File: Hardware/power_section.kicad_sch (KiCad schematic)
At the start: 40 parts, among them U4 TLV743P, U5 LM62440-Q1, U6 TLV743P, U7 TLV743P

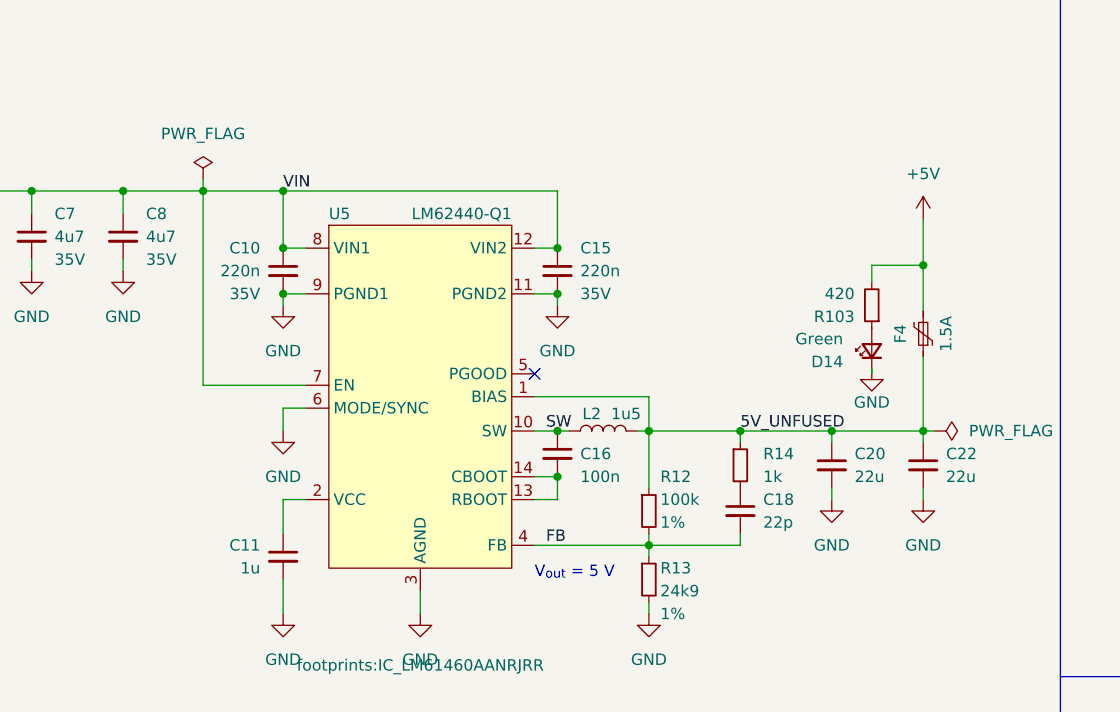
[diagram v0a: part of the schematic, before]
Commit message: Changes in current layout, added tensometers to layout
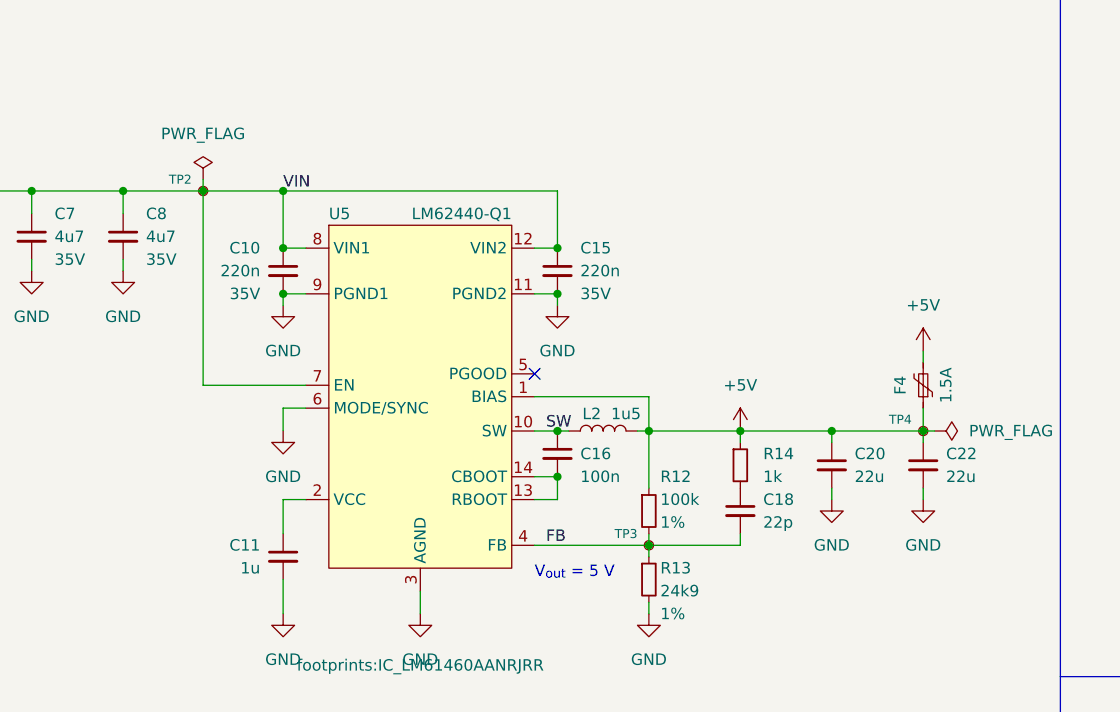
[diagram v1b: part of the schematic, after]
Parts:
- removed D14: Green, LED_SMD:LED_0603_1608Metric, symbol Device:LED_Small
- removed R103: 420, Resistor_SMD:R_0603_1608Metric, symbol Device:R_Small
- added TP2, TP3, TP4: TestPoint_Small, TestPoint:TestPoint_Pad_D1.0mm, symbol Connector:TestPoint_Small
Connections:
- net 5V_UNFUSED is gone; now on net +5V: C20.1, C22.1, F4.1, L2.2, R12.1, R14.1, U5.1 (BIAS)
- net +5V: now also TP4.1
- net FB: now also TP3.1
- net VIN: now also TP2.1
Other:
- moved on the sheet: F4

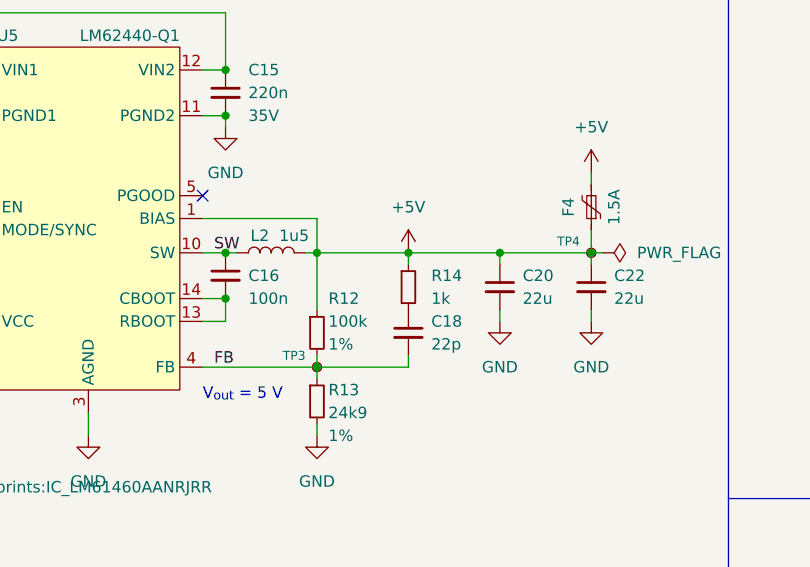
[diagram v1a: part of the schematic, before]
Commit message: Changes in power section
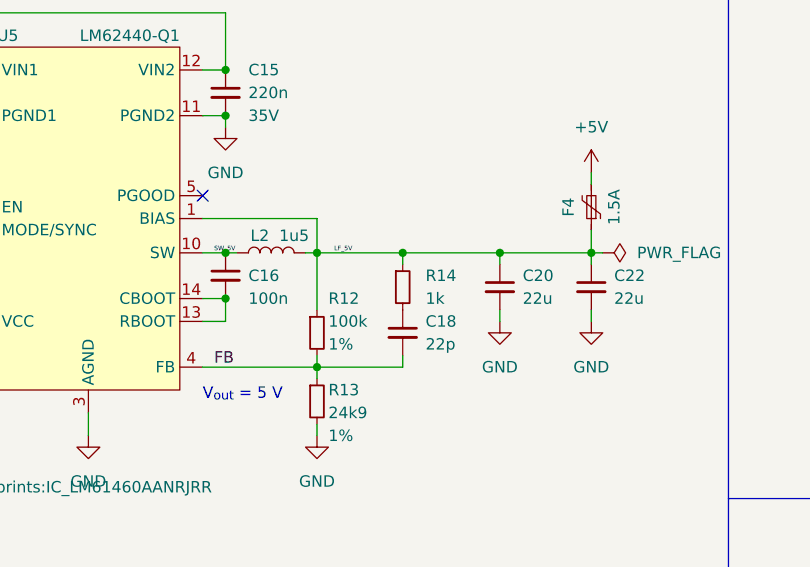
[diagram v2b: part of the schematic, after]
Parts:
- removed TP3, TP4: TestPoint_Small, TestPoint:TestPoint_Pad_D1.0mm, symbol Connector:TestPoint_Small
- TP2: footprint TestPoint:TestPoint_Pad_D1.0mm -> TestPoint:TestPoint_THTPad_D1.0mm_Drill0.5mm
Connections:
- net +5V: no longer C20.1, C22.1, F4.1, L2.2, R12.1, R14.1, U5.1 (BIAS)
- net SW renamed SW_5V
- new net LF_5V: C20.1, C22.1, F4.1, L2.2, R12.1, R14.1, U5.1 (BIAS)
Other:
- moved on the sheet: C18, R14
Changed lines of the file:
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@@
 	)
 	(junction
+		(at 140.97 64.77)
+		(diameter 0)
+		(color 0 0 0 0)
+	)
+	(junction
 		(at 58.42 158.75)
 		(diameter 0)
@@
 	)
 	(junction
-		(at 141.605 64.77)
-		(diameter 0)
-		(color 0 0 0 0)
-	)
-	(junction
 		(at 210.185 109.855)
 		(diameter 0)
@@
 	(wire
 		(pts
-			(xy 141.605 64.77) (xy 151.765 64.77)
-		)
-		(stroke
-			(width 0)
-			(type default)
-		)
-	)
-	(wire
-		(pts
 			(xy 195.58 116.205) (xy 195.58 116.84)
 		)
@@
 	(wire
 		(pts
-			(xy 141.605 64.77) (xy 141.605 66.04)
+			(xy 140.97 64.77) (xy 140.97 66.04)
 		)
 		(stroke
@@
 	(wire
 		(pts
+			(xy 140.97 64.77) (xy 151.765 64.77)
+		)
+		(stroke
+			(width 0)
+			(type default)
+		)
+	)
+	(wire
+		(pts
 			(xy 195.58 144.78) (xy 195.58 146.685)
 		)
@@
 	(wire
 		(pts
-			(xy 131.445 64.77) (xy 141.605 64.77)
+			(xy 131.445 64.77) (xy 140.97 64.77)
 		)
 		(stroke
@@
 	(wire
 		(pts
-			(xy 141.605 76.2) (xy 141.605 77.47)
+			(xy 140.97 76.2) (xy 140.97 77.47)
 		)
 		(stroke
@@
 	(wire
 		(pts
-			(xy 141.605 77.47) (xy 131.445 77.47)
+			(xy 140.97 77.47) (xy 131.445 77.47)
 		)
 		(stroke
@@
 		)
 	)
+	(label "LF_5V"
+		(at 133.35 64.77 0)
+		(fields_autoplaced yes)
+		(effects
+			(font
+				(size 0.5 0.5)
+			)
+			(justify left bottom)
+		)
+	)
 	(label "FB"
 		(at 120.015 77.47 0)
@@
 		)
 	)
-	(label "SW"
+	(label "SW_5V"
 		(at 120.015 64.77 0)
 		(fields_autoplaced yes)
 		(effects
 			(font
-				(size 1.27 1.27)
+				(size 0.5 0.5)
 			)
 			(justify left bottom)
@@
 	)
 	(symbol
-		(lib_id "power:+5V")
-		(at 141.605 64.77 0)
-		(unit 1)
-		(exclude_from_sim no)
-		(in_bom yes)
-		(on_board yes)
-		(dnp no)
-		(property "Reference" "#PWR0197"
-			(at 141.605 68.58 0)
-			(effects
-				(font
-					(size 1.27 1.27)
-				)
-				(hide yes)
-			)
-		)
-		(property "Value" "+5V"
-			(at 141.605 59.69 0)
-			(effects
-				(font
-					(size 1.27 1.27)
-				)
-			)
-		)
-		(property "Footprint" ""
-			(at 141.605 64.77 0)
-			(effects
-				(font
-					(size 1.27 1.27)
-				)
-				(hide yes)
-			)
-		)
-		(property "Datasheet" ""
-			(at 141.605 64.77 0)
-			(effects
-				(font
-					(size 1.27 1.27)
-				)
-				(hide yes)
-			)
-		)
-		(property "Description" ""
-			(at 141.605 64.77 0)
-			(effects
-				(font
-					(size 1.27 1.27)
-				)
-				(hide yes)
-			)
-		)
-		(pin "1"
-		)
-		(instances
-			(project "PUTM_EV_Frontbox_2023"
-				(path "/b652b05a-4e3d-4ad1-b032-18886abe7d45/fd3e8671-032e-4b6a-9a43-a9c36a92201e"
-					(reference "#PWR0197")
-					(unit 1)
-				)
-			)
-		)
-	)
-	(symbol
 		(lib_id "Regulator_Linear:TLV73330PDBV")
 		(at 220.345 147.32 0)
@@
 	)
 	(symbol
-		(lib_id "Connector:TestPoint_Small")
-		(at 161.925 64.77 0)
-		(unit 1)
-		(exclude_from_sim no)
-		(in_bom yes)
-		(on_board yes)
-		(dnp no)
-		(property "Reference" "TP4"
-			(at 160.655 63.5 0)
-			(effects
-				(font
-					(size 1 1)
-				)
-				(justify right)
-			)
-		)
-		(property "Value" "TestPoint_Small"
-			(at 163.195 66.675 0)
-			(effects
-				(font
-					(size 1.27 1.27)
-				)
-				(justify left)
-				(hide yes)
-			)
-		)
-		(property "Footprint" "TestPoint:TestPoint_Pad_D1.0mm"
-			(at 167.005 64.77 0)
-			(effects
-				(font
-					(size 1.27 1.27)
-				)
-				(hide yes)
-			)
-		)
-		(property "Datasheet" "~"
-			(at 167.005 64.77 0)
-			(effects
-				(font
-					(size 1.27 1.27)
-				)
-				(hide yes)
-			)
-		)
-		(property "Description" ""
-			(at 161.925 64.77 0)
-			(effects
-				(font
-					(size 1.27 1.27)
-				)
-				(hide yes)
-			)
-		)
-		(pin "1"
-		)
-		(instances
-			(project "PUTM_EV_Frontbox_2023"
-				(path "/b652b05a-4e3d-4ad1-b032-18886abe7d45/fd3e8671-032e-4b6a-9a43-a9c36a92201e"
-					(reference "TP4")
-					(unit 1)
-				)
-			)
-		)
-	)
-	(symbol
 		(lib_id "Regulator_Linear:TLV73330PDBV")
 		(at 47.625 161.29 0)
@@
 	(symbol
 		(lib_id "Device:R_Small")
-		(at 141.605 68.58 0)
+		(at 140.97 68.58 0)
 		(unit 1)
 		(exclude_from_sim no)
@@
 		(dnp no)
 		(property "Reference" "R14"
-			(at 144.145 67.31 0)
+			(at 143.51 67.31 0)
 			(effects
 				(font
@@
 		)
 		(property "Value" "1k"
-			(at 144.145 69.85 0)
+			(at 143.51 69.85 0)
 			(effects
 				(font
@@
 		)
 		(property "Footprint" "Resistor_SMD:R_0603_1608Metric"
-			(at 141.605 68.58 0)
+			(at 140.97 68.58 0)
 			(effects
 				(font
@@
 		)
 		(property "Datasheet" "~"
-			(at 141.605 68.58 0)
+			(at 140.97 68.58 0)
 			(effects
 				(font
@@
 		)
 		(property "Description" ""
-			(at 141.605 68.58 0)
+			(at 140.97 68.58 0)
 			(effects
 				(font
@@
 	)
 	(symbol
-		(lib_id "Connector:TestPoint_Small")
-		(at 131.445 77.47 0)
-		(unit 1)
-		(exclude_from_sim no)
-		(in_bom yes)
-		(on_board yes)
-		(dnp no)
-		(property "Reference" "TP3"
-			(at 130.175 76.2 0)
-			(effects
-				(font
-					(size 1 1)
-				)
-				(justify right)
-			)
-		)
-		(property "Value" "TestPoint_Small"
-			(at 132.715 79.375 0)
-			(effects
-				(font
-					(size 1.27 1.27)
-				)
-				(justify left)
-				(hide yes)
-			)
-		)
-		(property "Footprint" "TestPoint:TestPoint_Pad_D1.0mm"
-			(at 136.525 77.47 0)
-			(effects
-				(font
-					(size 1.27 1.27)
-				)
-				(hide yes)
-			)
-		)
-		(property "Datasheet" "~"
-			(at 136.525 77.47 0)
-			(effects
-				(font
-					(size 1.27 1.27)
-				)
-				(hide yes)
-			)
-		)
-		(property "Description" ""
-			(at 131.445 77.47 0)
-			(effects
-				(font
-					(size 1.27 1.27)
-				)
-				(hide yes)
-			)
-		)
-		(pin "1"
-		)
-		(instances
-			(project "PUTM_EV_Frontbox_2023"
-				(path "/b652b05a-4e3d-4ad1-b032-18886abe7d45/fd3e8671-032e-4b6a-9a43-a9c36a92201e"
-					(reference "TP3")
-					(unit 1)
-				)
-			)
-		)
-	)
-	(symbol
 		(lib_id "power:+5V")
 		(at 33.655 156.845 0)
@@
 			)
 		)
-		(property "Footprint" "TestPoint:TestPoint_Pad_D1.0mm"
+		(property "Footprint" "TestPoint:TestPoint_THTPad_D1.0mm_Drill0.5mm"
 			(at 86.995 38.1 0)
 			(effects
@@
 	(symbol
 		(lib_id "Device:C_Small")
-		(at 141.605 73.66 0)
+		(at 140.97 73.66 0)
 		(mirror y)
 		(unit 1)
@@
 		(dnp no)
 		(property "Reference" "C18"
-			(at 144.145 72.39 0)
+			(at 143.51 72.39 0)
 			(effects
 				(font
@@
 		)
 		(property "Value" "22p"
-			(at 144.145 74.93 0)
+			(at 143.51 74.93 0)
 			(effects
 				(font
@@
 		)
 		(property "Footprint" "Capacitor_SMD:C_0603_1608Metric"
-			(at 141.605 73.66 0)
+			(at 140.97 73.66 0)
 			(effects
 				(font
@@
 		)
 		(property "Datasheet" "~"
-			(at 141.605 73.66 0)
+			(at 140.97 73.66 0)
 			(effects
 				(font
@@
 		)
 		(property "Description" ""
-			(at 141.605 73.66 0)
+			(at 140.97 73.66 0)
 			(effects
 				(font

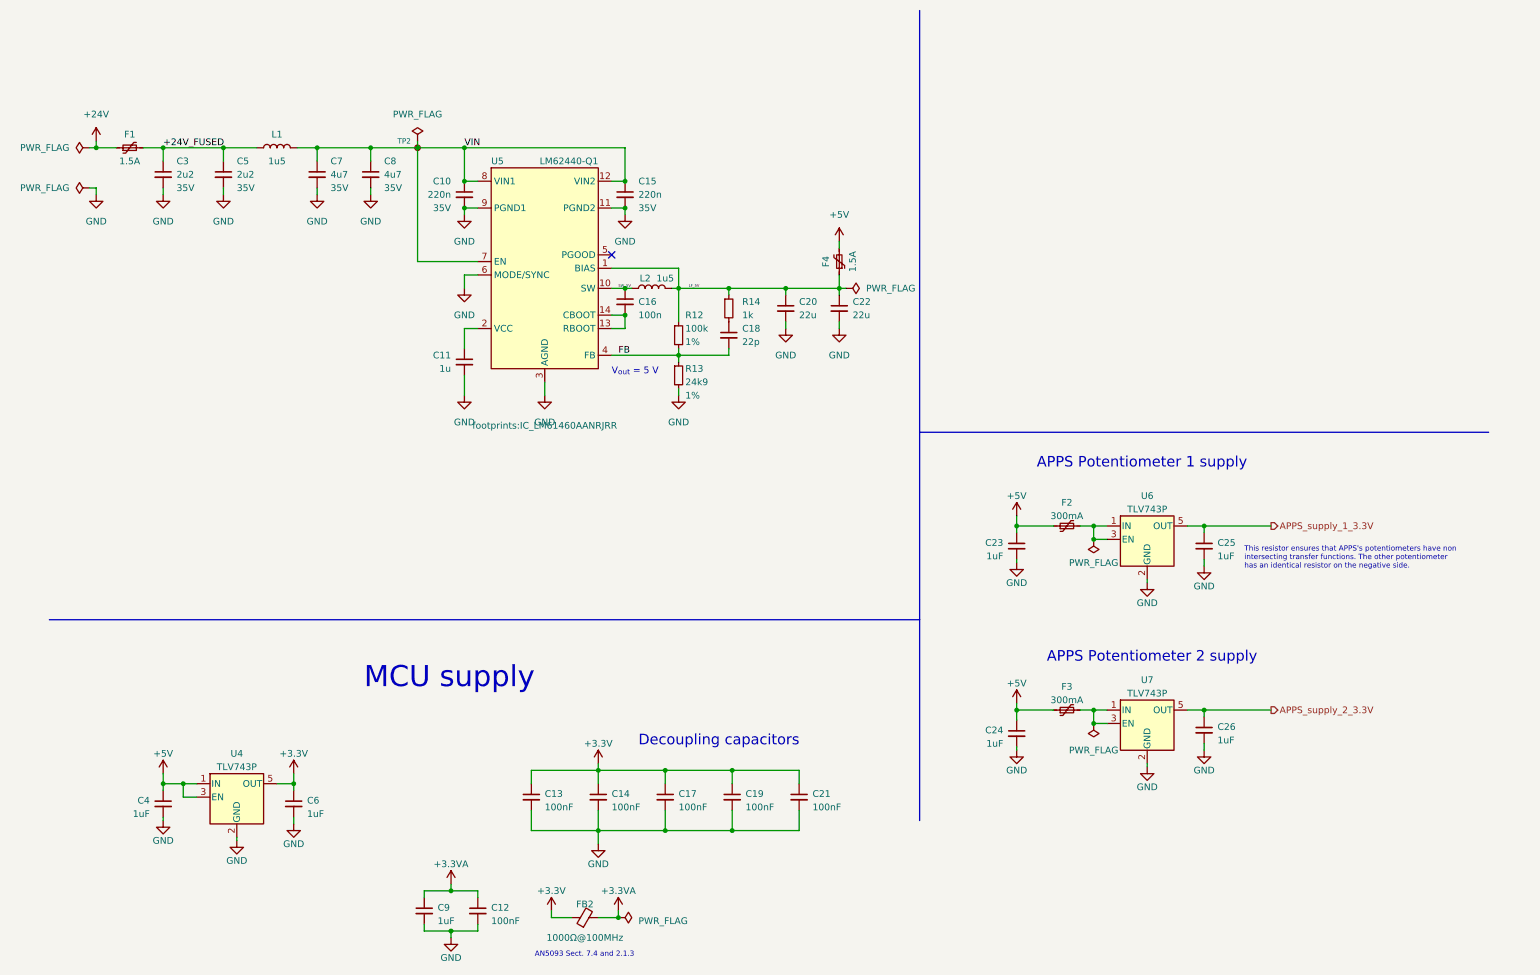
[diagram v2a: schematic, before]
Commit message: Converter change
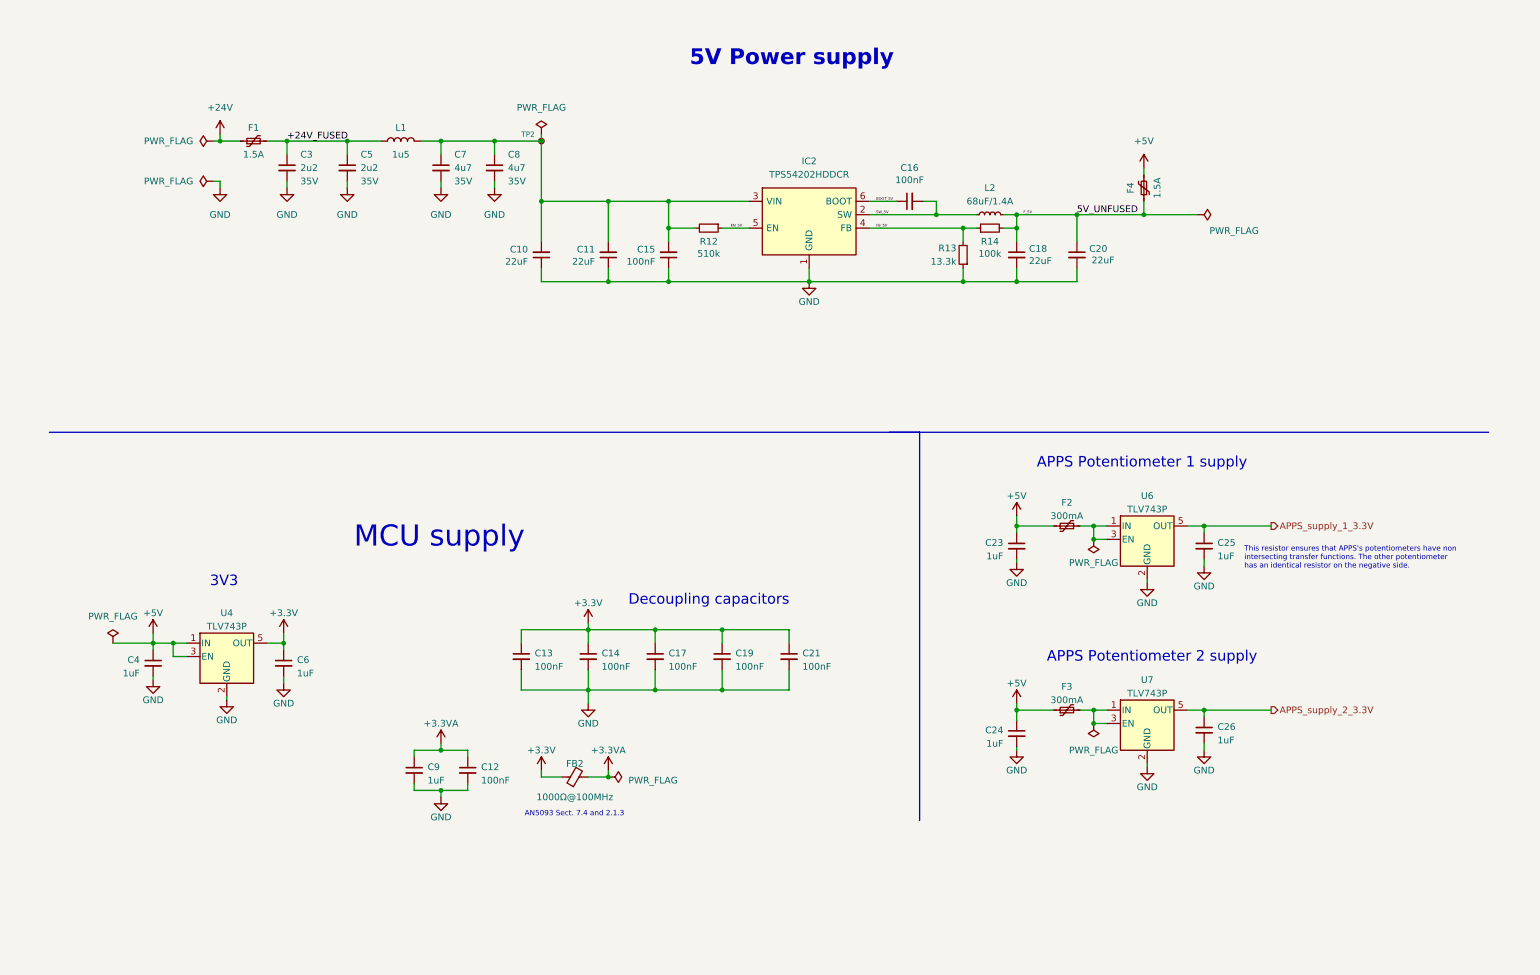
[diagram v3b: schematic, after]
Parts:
- removed C22: 22u, Capacitor_SMD:C_0603_1608Metric, symbol Device:C_Small
- removed L2: 1u5, Inductor_SMD:L_Abracon_ASPI-4030S, symbol Device:L
- removed U5: LM62440-Q1, footprints:IC_LM61460AANRJRR, symbol LM62440:LM62440
- added IC2: TPS54202HDDCR, Package_TO_SOT_SMD:SOT-23-6, symbol SamacsysNew:TPS54202HDDCR
- added L2: 68uF/1.4A, Inductor_SMD:L_TDK_VLS6045EX_VLS6045AF, symbol Samacsys_kicad_sym:SRR4028-271Y
- C10: value 220n -> 22uF; Manufacturer_Name (none) -> MCASH21GCC7684MTCA1J; Manufacturer_Part_Number (none) -> CL21A107MQYNNWE; Mouser Part Number (none) -> 810-C2012X5R1V226MAC; Rated Voltage 35V -> (none)
- C11: value 1u -> 22uF; footprint Capacitor_SMD:C_0603_1608Metric -> Capacitor_SMD:C_0805_2012Metric; Manufacturer_Name (none) -> MCASH21GCC7684MTCA1J; Manufacturer_Part_Number (none) -> CL21A107MQYNNWE; Mouser Part Number (none) -> 810-C2012X5R1V226MAC
- C15: value 220n -> 100nF; footprint Capacitor_SMD:C_0805_2012Metric -> Capacitor_SMD:C_0603_1608Metric; Manufacturer_Name (none) -> --; Manufacturer_Part_Number (none) -> C0603C104J3RACTU; Mouser Part Number (none) -> --; Mouser Price/Stock (none) -> https://www.mouser.pl/ProductDetail/KEMET/C0603C104J3RACTU?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; Rated Voltage 35V -> (none)
- C16: value 100n -> 100nF; Manufacturer_Name (none) -> --; Manufacturer_Part_Number (none) -> C0603C104J3RACTU; Mouser Part Number (none) -> --; Mouser Price/Stock (none) -> https://www.mouser.pl/ProductDetail/KEMET/C0603C104J3RACTU?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
- C18: value 22p -> 22uF; footprint Capacitor_SMD:C_0603_1608Metric -> Capacitor_SMD:C_0805_2012Metric; Manufacturer_Name (none) -> MCASH21GCC7684MTCA1J; Manufacturer_Part_Number (none) -> CL21A107MQYNNWE; Mouser Part Number (none) -> 810-C2012X5R1V226MAC
- C20: value 22u -> 22uF; footprint Capacitor_SMD:C_0603_1608Metric -> Capacitor_SMD:C_0805_2012Metric; Manufacturer_Name (none) -> MCASH21GCC7684MTCA1J; Manufacturer_Part_Number (none) -> CL21A107MQYNNWE; Mouser Part Number (none) -> 810-C2012X5R1V226MAC
- R12: value 100k -> 510k; Manufacturer_Name (none) -> --; Manufacturer_Part_Number (none) -> RT0603DRD07510KL; Mouser Part Number (none) -> 603-RT0603DRD07510KL; Mouser Price/Stock (none) -> https://www.mouser.pl/ProductDetail/YAGEO/RT0603DRD07510KL?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; Tolerance 1% -> (none)
- R13: value 24k9 -> 13.3k; Manufacturer_Name (none) -> --; Manufacturer_Part_Number (none) -> RT0603DRE0713K3L; Mouser Part Number (none) -> 603-RT0603DRE0713K3L; Mouser Price/Stock (none) -> https://www.mouser.pl/ProductDetail/YAGEO/RT0603DRE0713K3L?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; Tolerance 1% -> (none)
- R14: value 1k -> 100k; Manufacturer_Name (none) -> --; Manufacturer_Part_Number (none) -> RT0603DRE07100KL; Mouser Part Number (none) -> --; Mouser Price/Stock (none) -> https://www.mouser.pl/ProductDetail/YAGEO/RT0603DRE07100KL?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
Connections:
- net GND: now also C10.1, C11.1, C15.1, C18.2, R13.1, IC2.1 (GND); no longer C10.2, C11.2, C15.2, R13.2
- net SW_5V: now also C16.2, IC2.2 (SW), L2.1; no longer C16.1
- net 5V_UNFUSED: now reaches C18.1, R14.2
- net 5V_UNFUSED: now also C20.1, F4.1, L2.2
- removed net FB: C18.2, R12.2, R13.1
- removed net LF_5V: C20.1, F4.1, R12.1, R14.1
- net VIN: no longer names the net of C7.1, C8.1, L1.2, TP2.1
- net VIN: now also C10.2, C11.2, C15.2, R12.2, IC2.3 (VIN); no longer C10.1, C15.1
- new net BOOT_5V: C16.1, IC2.6 (BOOT)
- new net EN_5V: IC2.5 (EN), R12.1
- new net FB_5V: IC2.4 (FB), R13.2, R14.1
- no-connect marks 1 -> 0
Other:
- note added: "3V3"
- note added: "5V Power supply"
- note removed: "V_{out} = 5 V"
- moved on the sheet: C12, C13, C14, C17, C19, C21, C3, C4, C5, C6, C7, C8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
